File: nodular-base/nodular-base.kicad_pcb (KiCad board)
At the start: 4 copper layers, 83.1 x 92.5 mm, 161 parts, among them J1 Conn_02x10_Counter_Clockwise, J10 Conn_01x02_MountingPin, J11 Conn_01x08_Pin, J2 Conn_02x10_Counter_Clockwise, J3 Conn_02x10_Counter_Clockwise, J4 Conn_02x10_Counter_Clockwise, J5 Conn_02x10_Counter_Clockwise, J6 Conn_02x10_Counter_Clockwise, J7 USB_C_Receptacle_USB2.0, J8 USB_C_Receptacle_USB2.0, J9 Conn_01x30_MountingPin, SW1 SW_Push, SW2 SW_Push, SW3 SW_Push, U1 ESP32-S3-PICO-1-N8R2, U10 MT9700, U11 MT9700, U12 MT9700, U13 MT9700, U14 MT9700, U15 74LVC1G04, U16 RCLAMP0524P-ES, U17 RCLAMP0524P-ES, U18 RCLAMP0524P-ES, U19 74LVC1G04, U2 FUSB302BMPX, U20 RCLAMP0524P-ES, U21 RCLAMP0524P-ES, U22 RCLAMP0524P-ES, U23 74LVC1G04, U24 AW9523B, U25 AW9523B, U26 AW9523B, U27 RCLAMP0524P-ES, U28 RCLAMP0524P-ES, U29 RCLAMP0524P-ES, U3 BQ25895RTW, U30 RCLAMP0524P-ES, U31 74LVC1G04, U32 74LVC1G04, U33 74LVC1G04, U34 RCLAMP0524P-ES, U35 RCLAMP0524P-ES, U36 RCLAMP0524P-ES, U37 RCLAMP0524P-ES, U38 RCLAMP0524P-ES, U39 RCLAMP0524P-ES, U4 TCA9548APWR, U40 RCLAMP0524P-ES, U41 RCLAMP0524P-ES, U42 RCLAMP0524P-ES, U43 TLV62595DMQR, U44 RCLAMP0524P-ES, U45 RCLAMP0524P-ES, U46 RCLAMP0524P-ES, U47 RCLAMP0524P-ES, U48 RCLAMP0524P-ES, U49 RCLAMP0524P-ES, U5 FUSB302BMPX, U50 TS3USB221A, U6 74LVC1G17, U7 SC7A20, U8 MT9700, U9 MT9700

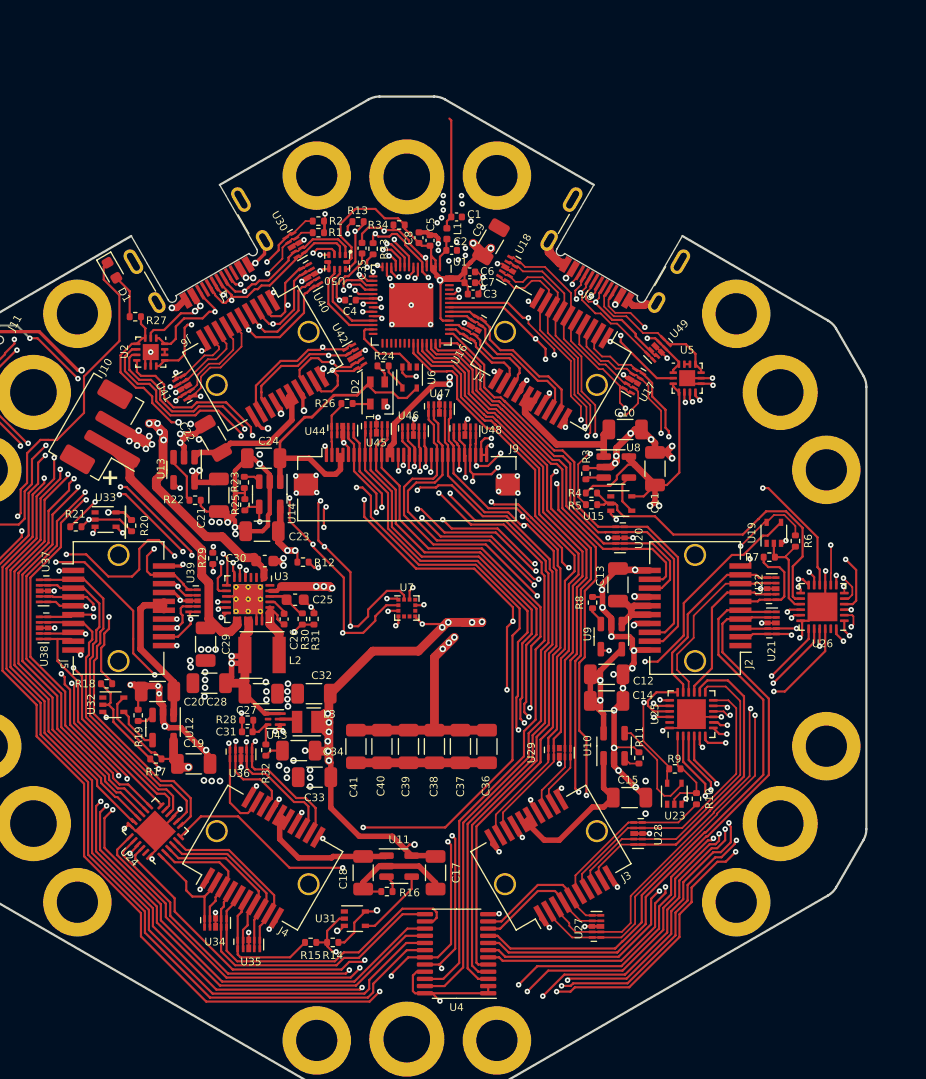
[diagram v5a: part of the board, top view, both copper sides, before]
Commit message: Add hole Add decoupling caps, pullups, and voltage dividers Set current limit on PMIC Determine battery attachment angle Update BOM and pinouts
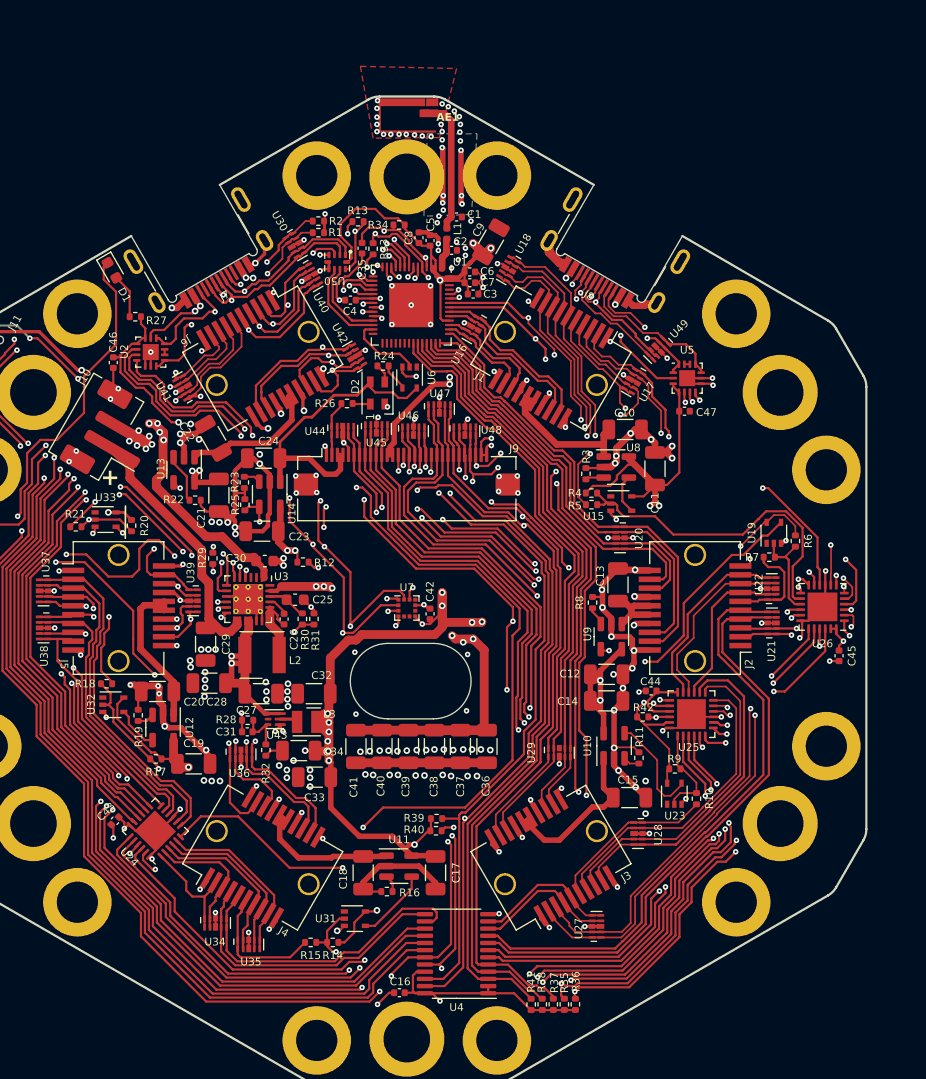
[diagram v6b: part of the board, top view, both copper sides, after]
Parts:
- added AE1: 2450AT07A0100, nodular:Johanson_2450AT07A0100_FLRight, F.Cu at (101.7, 54.8)
- added C16: 100nF, Capacitor_SMD:C_0402_1005Metric, F.Cu at (99.3, 134.8)
- added C42: 100nF, Capacitor_SMD:C_0402_1005Metric, F.Cu at (102.1, 100.5)
- added C43: 100nF, Capacitor_SMD:C_0402_1005Metric, F.Cu at (73.6, 119.2)
- added C44: 100nF, Capacitor_SMD:C_0402_1005Metric, F.Cu at (122.1, 107.5)
- added C45: 100nF, Capacitor_SMD:C_0402_1005Metric, F.Cu at (139.1, 104.3)
- added C46: 100nF, Capacitor_SMD:C_0402_1005Metric, F.Cu at (73.5, 77.8)
- added C47: 100nF, Capacitor_SMD:C_0402_1005Metric, F.Cu at (125.1, 82.2)
- added R35: 2k2, Resistor_SMD:R_0402_1005Metric, F.Cu at (114.2, 135.8)
- added R36: 2k2, Resistor_SMD:R_0402_1005Metric, F.Cu at (115.2, 135.8)
- added R37: 2k2, Resistor_SMD:R_0402_1005Metric, F.Cu at (113.2, 135.8)
- added R38: 2k2, Resistor_SMD:R_0402_1005Metric, F.Cu at (112.2, 135.8)
- added R39: 2k2, Resistor_SMD:R_0402_1005Metric, F.Cu at (102.7, 119.0)
- added R40: 2k2, Resistor_SMD:R_0402_1005Metric, F.Cu at (102.6, 120.2)
- added R41: 10k, Resistor_SMD:R_0402_1005Metric, F.Cu at (111.2, 135.9)
- added R42: 10k, Resistor_SMD:R_0402_1005Metric, F.Cu at (121.3, 109.8)
- C31: value 47nF -> 120pF
- J10: footprint Connector_JST:JST_PH_B2B-PH-SM4-TB_1x02-1MP_P2.00mm_Vertical -> nodular:JST_PH_B2B-PH-SM4-TB_1x02-1MP_P2.00mm_Vertical
- R28: value R -> 45k
- R29: value 10k -> 260R
- R32: value R -> 10k
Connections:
- U24 pad 23: unconnected-(U24-~{RST}-Pad23) -> 3V3_SYS
- U25 pad 23: unconnected-(U25-~{RST}-Pad23) -> 3V3_SYS
- U26 pad 23: unconnected-(U26-~{RST}-Pad23) -> 3V3_SYS
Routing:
- net 3V3_SYS: track 473.3 -> 506.2 mm, vias 39 -> 41
- net GND: track 303.9 -> 321.6 mm, vias 200 -> 260
- net /USB/PMID: track 97.4 -> 105.3 mm
- net /SCL_TOP: track 89.6 -> 96.9 mm
- net /SDA_TOP: track 90.4 -> 96.3 mm
- net /I2C_RESET: track 81.1 -> 85.7 mm
- net /SDA_HOST: track 75.0 -> 77.8 mm, vias 2 -> 4
- net /SCL_SYS: track 202.9 -> 205.0 mm
- net /SCL_HOST: track 75.7 -> 77.4 mm
- net /SDA_SYS: track 202.2 -> 203.7 mm
- net Net-(AE1-FEED): track 10.2 -> 11.5 mm
- net /GPIO/DET_F: track 133.6 -> 133.1 mm
- net /~{INT_SYS}: track 248.3 -> 248.8 mm
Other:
- outline, holes or cut-outs redrawn

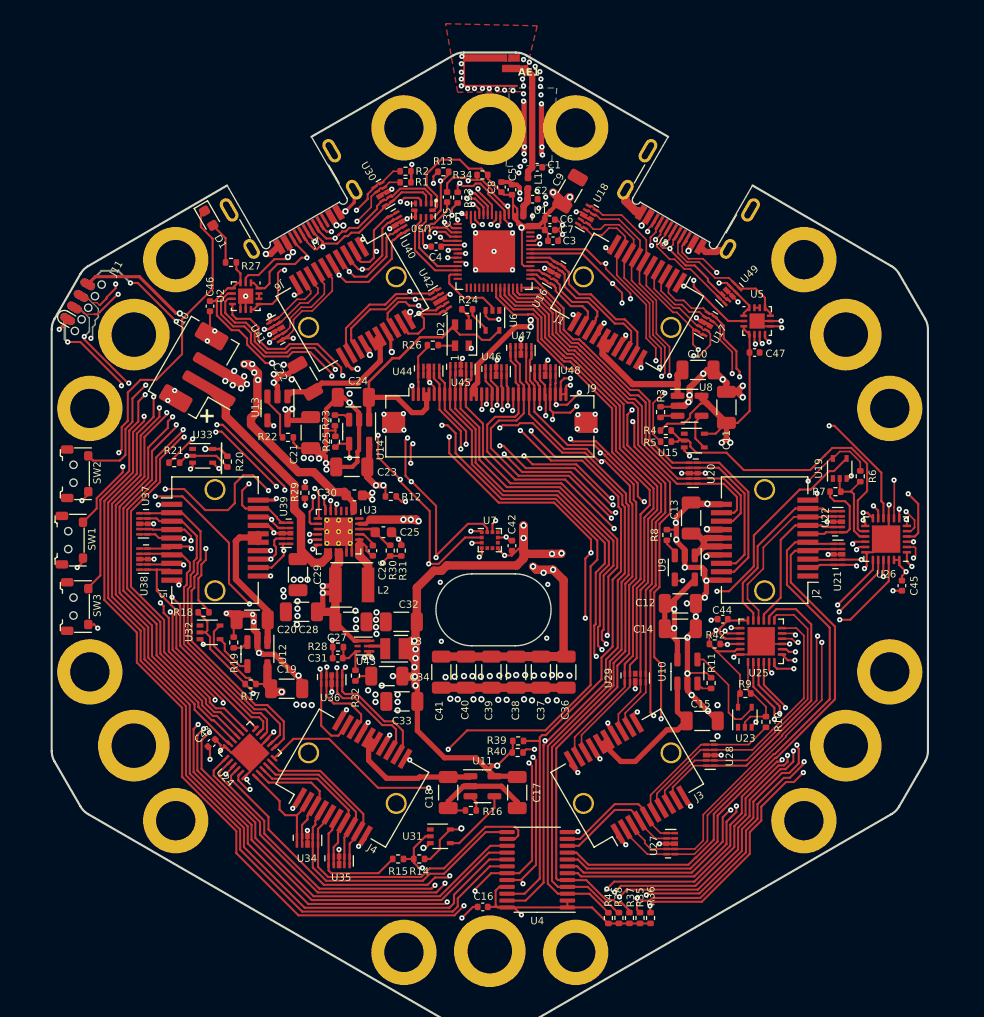
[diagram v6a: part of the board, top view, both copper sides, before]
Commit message: Add VCONN support and load switch with 1.5A current limit on host port Add accelerometer interrupt connection Update BOM with important capacitor and inductor PNs and costings
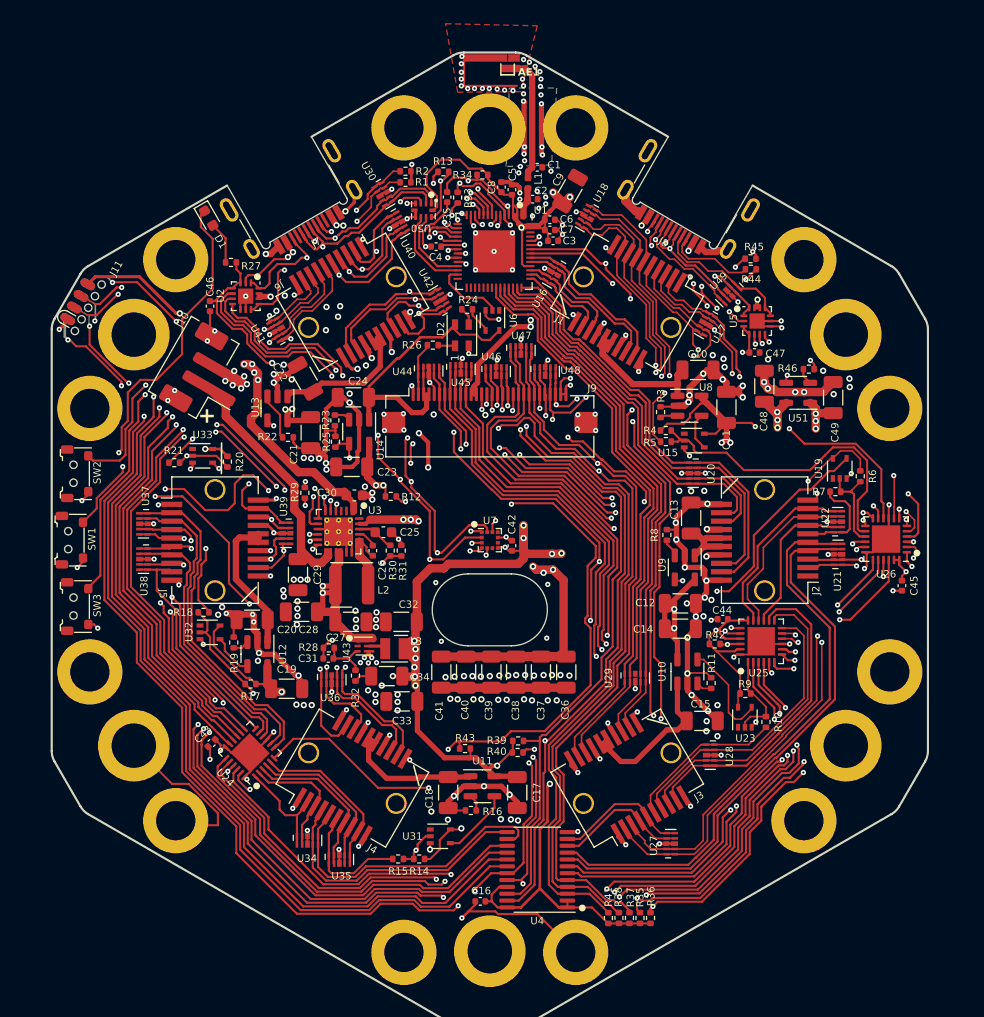
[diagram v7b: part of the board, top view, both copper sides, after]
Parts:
- added C48: 10uF, Capacitor_SMD:C_1206_3216Metric, F.Cu at (126.0, 85.4)
- added C49: 10uF, Capacitor_SMD:C_1206_3216Metric, F.Cu at (132.6, 86.5)
- added R43: 10k, Resistor_SMD:R_0402_1005Metric, F.Cu at (97.7, 119.8)
- added R44: 260R, Resistor_SMD:R_0402_1005Metric, F.Cu at (124.8, 74.3)
- added R45: 260R, Resistor_SMD:R_0402_1005Metric, F.Cu at (124.7, 73.3)
- added R46: 4.3k, Resistor_SMD:R_0402_1005Metric, F.Cu at (130.3, 83.8)
- added U51: MT9700, Package_TO_SOT_SMD:SOT-23-5, F.Cu at (129.3, 86.0)
- L2: value L -> YHNR4020-2R2M
- L3: value L -> FTC252010SR47MBCA
- moved C31 0.90 mm to (84.7, 111.2)
- moved R28 0.88 mm to (84.7, 110.2)
- moved C16 0.57 mm to (99.1, 134.3)
- moved U35 0.14 mm to (85.7, 130.3)
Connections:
- J8 pad A4: /USB/PMID -> /USB/PMID_SW
- J8 pad A8: /ESP_TXD -> /USB/TX
- J8 pad A9: /USB/PMID -> /USB/PMID_SW
- J8 pad B4: /USB/PMID -> /USB/PMID_SW
- J8 pad B8: /ESP_RXD -> /USB/RX
- J8 pad B9: /USB/PMID -> /USB/PMID_SW
- U2 pad 12: Net-(U2-VCONN-Pad12) -> /USB/PMID
- U2 pad 13: Net-(U2-VCONN-Pad12) -> /USB/PMID
- U24 pad 6: unconnected-(U24-P0_1-Pad6) -> /INT_ACCEL
- U26 pad 10: unconnected-(U26-P0_4-Pad10) -> /VBUS_SW
- U44 pad 2: Net-(U44-CHB-Pad2) -> /bot-top-link/TOP_VBAT_SW
- U44 pad 9: Net-(U44-CHB-Pad2) -> /bot-top-link/TOP_VBAT_SW
- U5 pad 12: Net-(U5-VCONN-Pad12) -> /USB/PMID
- U5 pad 13: Net-(U5-VCONN-Pad12) -> /USB/PMID
- U5 pad 2: /USB/PMID -> /USB/PMID_SW
- U7 pad 5: unconnected-(U7-INT1-Pad5) -> /INT_ACCEL
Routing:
- net unconnected-(U24-P0_1-Pad6): track 72.2 -> 0.00 mm, vias 3 -> 0
- net /INT_ACCEL: track 0.00 -> 69.9 mm, vias 0 -> 4
- net /USB/PMID_SW: track 0.00 -> 46.9 mm, vias 0 -> 6
- net GND: track 321.6 -> 362.8 mm, vias 260 -> 302
- net /USB/PMID: track 105.3 -> 140.9 mm, vias 9 -> 14
- net /VBUS_SW: track 0.00 -> 21.0 mm, vias 0 -> 2
- net /USB/TX: track 0.00 -> 15.6 mm, vias 0 -> 2
- net unconnected-(U26-P0_4-Pad10): track 11.2 -> 0.00 mm, vias 1 -> 0
- net /USB/RX: track 0.00 -> 8.38 mm
- net /ESP_TXD: track 117.6 -> 110.6 mm, vias 9 -> 10
- net /VSYS: track 41.2 -> 44.3 mm
- net /bot-top-link/TOP_VBAT_SW: track 27.0 -> 29.4 mm
- net /SDA_TOP: track 96.3 -> 94.4 mm
- net /I2C_RESET: track 85.7 -> 87.5 mm
- net Net-(U51-SET): track 0.00 -> 1.57 mm
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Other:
- outline, holes or cut-outs redrawn
